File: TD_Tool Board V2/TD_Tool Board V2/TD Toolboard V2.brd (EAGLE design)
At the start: 54.2 x 49 mm, 141 parts, among them J3 430450400CON_430450400_MOL, M1 NMOSFET_WSD3066DN33, M2 CJ3400, M3 CJ3400, M4 CJ3400, P1 TPS54202_BUCKCONV, P2 3.3V, U1 RP2040IC57_RP2040-L, U2 W25Q128JVSIQSOIC_128JVSIQ_WIN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, U3 SN65HVD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

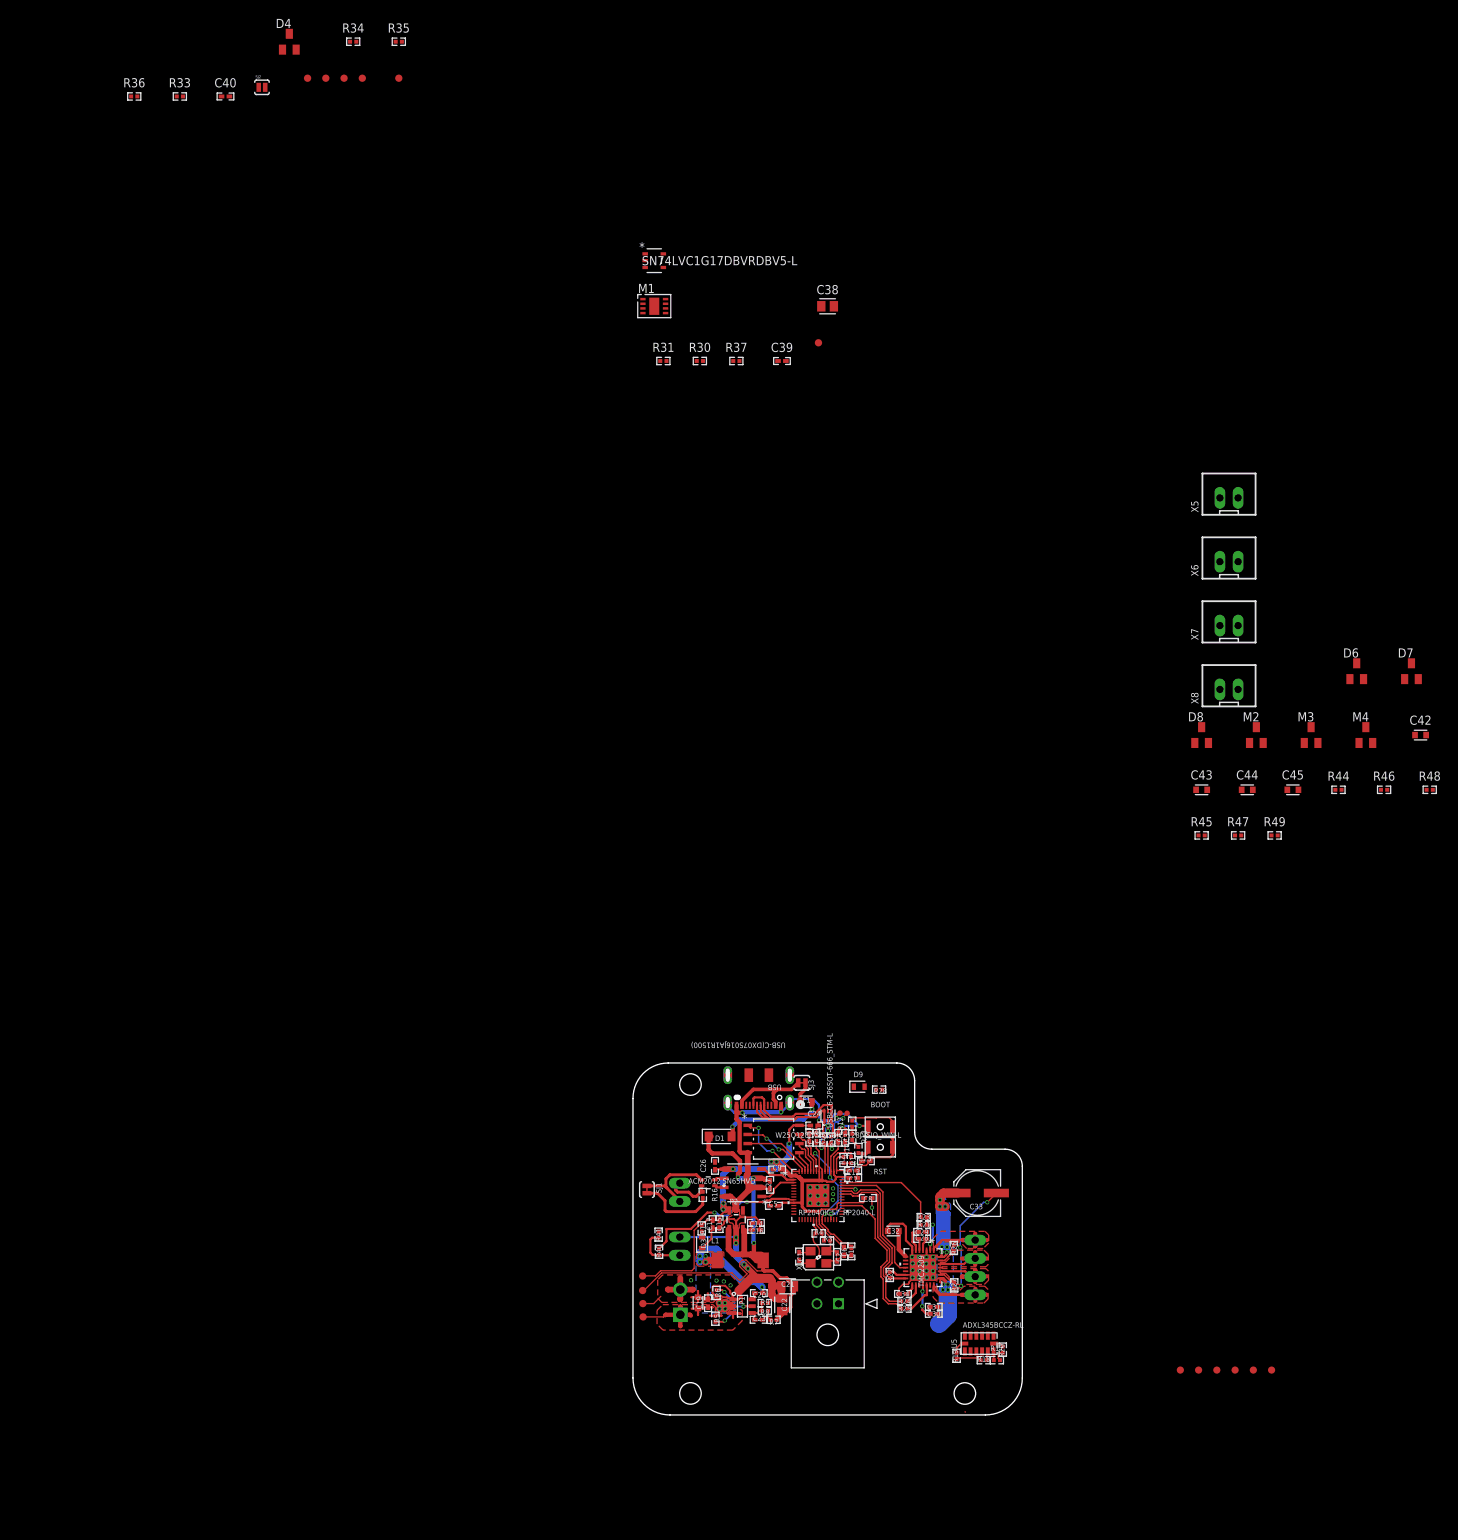
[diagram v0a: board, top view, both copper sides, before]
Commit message: Placed other connectors and re arranged adxl345
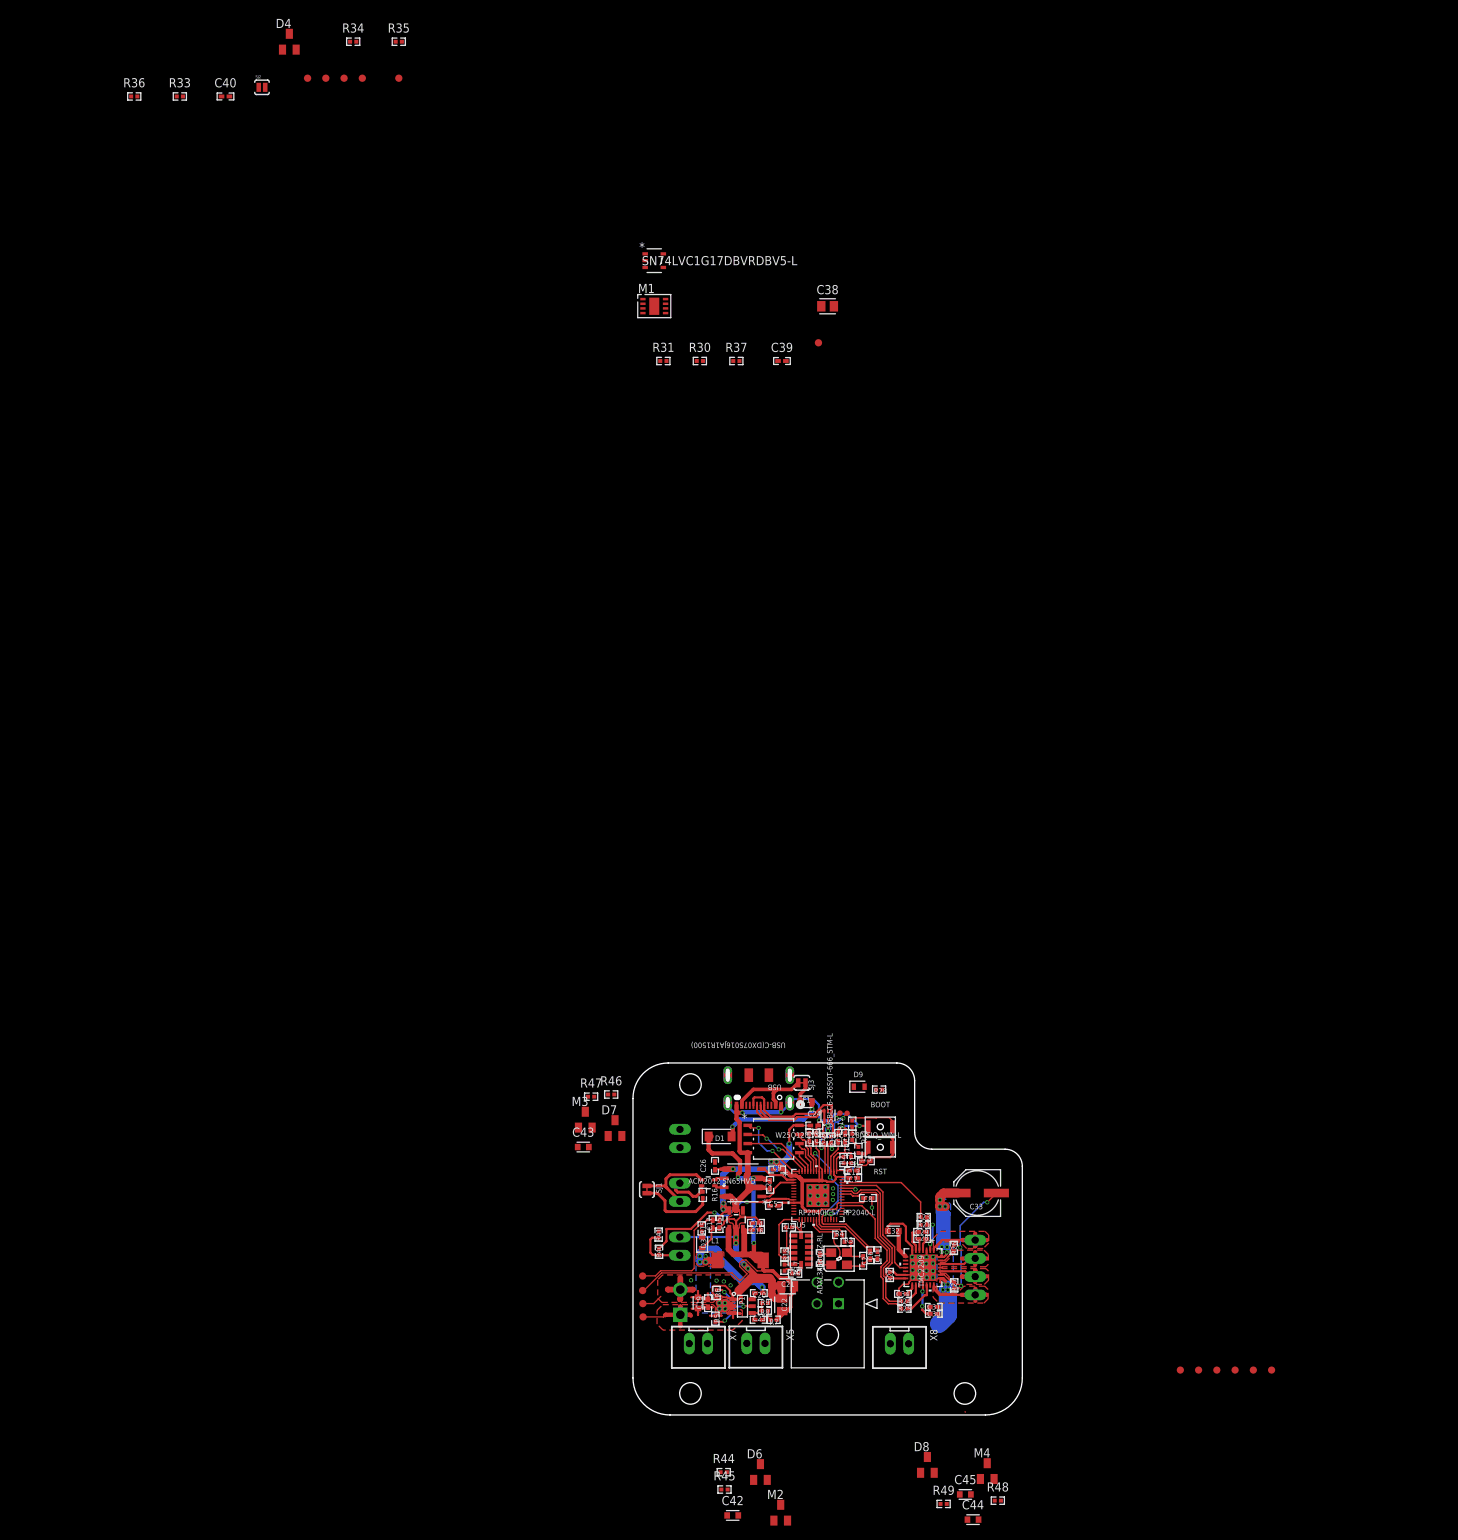
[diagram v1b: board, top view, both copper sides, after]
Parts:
- moved C42 144.8 mm to (104.9, -71.8)
- moved D6 139.0 mm to (108.8, -65.8)
- moved X5 134.9 mm to (108.1, -47.9), turned to 180 degrees
- moved R44 127.9 mm to (103.7, -65.8)
- moved D7 127.8 mm to (88.5, -17.9)
- moved M2 126.9 mm to (111.6, -71.4)
- moved X7 124.3 mm to (100.1, -47.9), turned to 180 degrees
- moved R48 115.8 mm to (141.8, -69.7)
- moved R46 115.7 mm to (88.0, -13.2)
- moved M4 115.2 mm to (140.3, -65.6)
- moved M3 114.4 mm to (84.4, -16.7)
- moved R45 112.7 mm to (103.8, -68.2)
- moved X6 110.8 mm to (97.6, -19.3), flipped to the bottom, turned to 270 degrees
- moved C44 108.5 mm to (138.4, -72.4)
- moved D8 108.5 mm to (132.0, -64.8)
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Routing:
- net SPI1_MISO: track 1.27 -> 9.50 mm
- net +3.3V: track 116.9 -> 120.6 mm
- net +1.1V: track 28.2 -> 31.8 mm
- net OSC_OUT: track 3.29 -> 6.21 mm
- net OSC_IN: track 8.41 -> 10.8 mm
- net SPI1_CS: track 1.95 -> 3.72 mm
- net XR: track 3.26 -> 4.16 mm
- net GND: track 195.9 -> 196.7 mm

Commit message: Finished routing all components
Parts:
- removed FD1, FD2, FD3: FIDUCIAL, CDC Library:FIDUCIAL_1MM
- D9: device LED:LEDC1608X35N_FLAT-G -> led:LED3MM
- moved FD5 178.9 mm to (8.90, 8.55)
- moved FD6 172.4 mm to (41.6, 51.4)
- moved C44 145.2 mm to (17.6, 8.18), turned to 270 degrees
- moved FD4 134.2 mm to (55.2, 9.11)
- moved R48 128.0 mm to (39.9, 7.77), turned to 180 degrees
- moved C45 125.8 mm to (39.5, 10.3)
- moved R49 123.1 mm to (39.9, 8.86), turned to 180 degrees
- moved M4 120.7 mm to (45.6, 9.19)
- moved C42 118.3 mm to (19.8, 10.4), turned to 180 degrees
- moved M2 117.6 mm to (26.0, 9.14)
- moved D8 116.0 mm to (42.6, 9.17), turned to 180 degrees
- moved D6 114.0 mm to (22.9, 9.22), turned to 180 degrees
- moved R45 113.7 mm to (20.0, 8.69), turned to 180 degrees
- moved R20 111.7 mm to (26.4, 31.6)
- moved R44 111.4 mm to (20.0, 7.72), turned to 180 degrees
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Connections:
- net GND: now also D9.K; no longer D9.C
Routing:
- net +3.3V: track 120.6 -> 256.3 mm, vias 6 -> 17
- net +24V: track 45.9 -> 176.4 mm, vias 11 -> 13
- net N$2: track 0.00 -> 38.5 mm
- net HE0: track 0.00 -> 37.2 mm, vias 0 -> 2
- net FAN2: track 0.00 -> 36.6 mm, vias 0 -> 2
- net FAN0: track 0.00 -> 33.2 mm, vias 0 -> 2
- net FAN1: track 0.00 -> 32.8 mm, vias 0 -> 2
- net LED: track 0.00 -> 29.2 mm, vias 0 -> 3
- net TH0: track 1.95 -> 29.3 mm, vias 1 -> 3
- net TH0A: track 0.00 -> 26.6 mm, vias 0 -> 1
- net HE0_PWR: track 0.00 -> 25.7 mm
- net +5V: track 76.5 -> 100.1 mm
- net GND: track 196.7 -> 216.6 mm, vias 49 -> 211
- net QSPI_SS: track 12.0 -> 25.2 mm, vias 2 -> 4
- net FAN1G: track 0.00 -> 8.34 mm
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- added copper zone on layer 1, net HE0_PWR
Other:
- outline, holes or cut-outs redrawn
- board text removed: "Fans"
- board text removed: "Hotend Heater"
- board text removed: "Stepper Driver"
- board text removed: "Toolhead Connectors"
- board text removed: "USB"
- board text removed: "Umblical Connectors"

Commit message: Minor Changes for ground connectivity
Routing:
- net TH0A: track 26.6 -> 23.7 mm
- net +5V: track 100.1 -> 97.3 mm
- net FAN1: track 32.8 -> 34.3 mm
- net +3.3V: track 256.3 -> 255.0 mm
- net GND: track 216.6 -> 216.7 mm, vias 211 -> 213

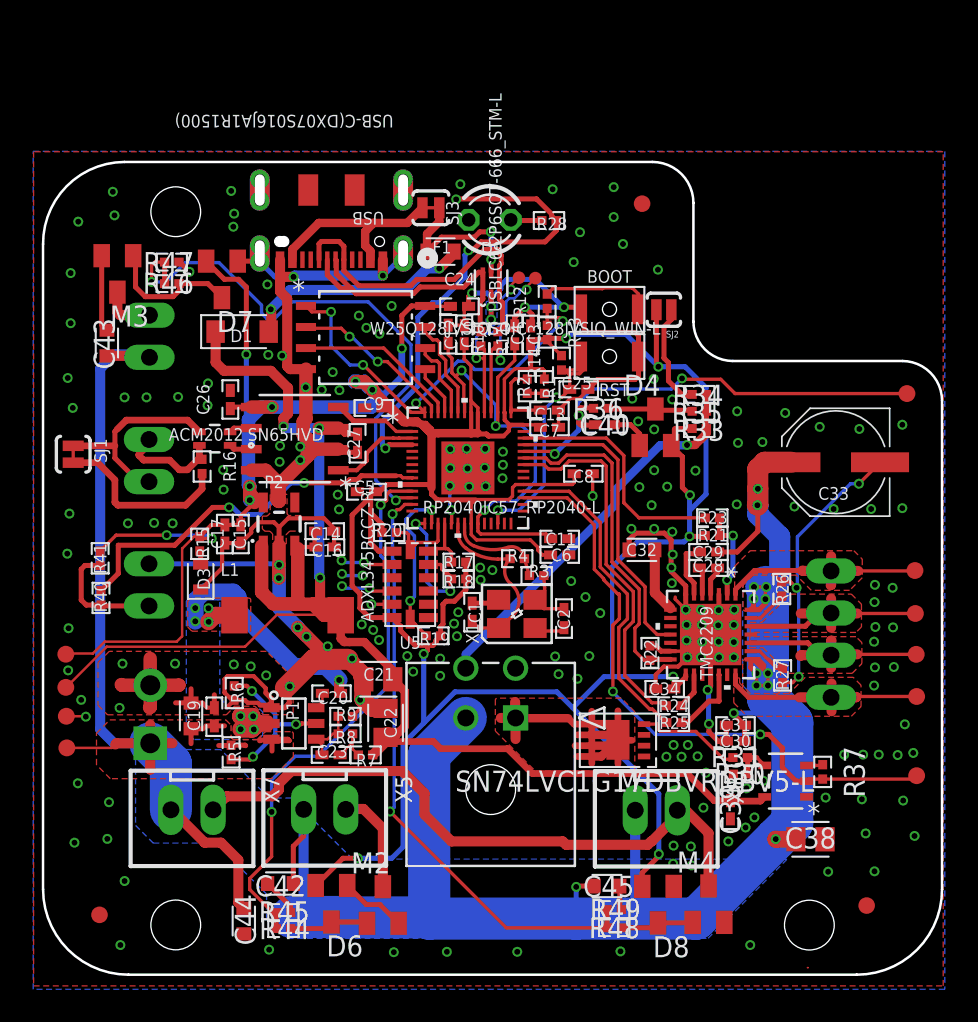
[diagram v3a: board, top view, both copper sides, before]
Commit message: Fixed font sizes, added lables
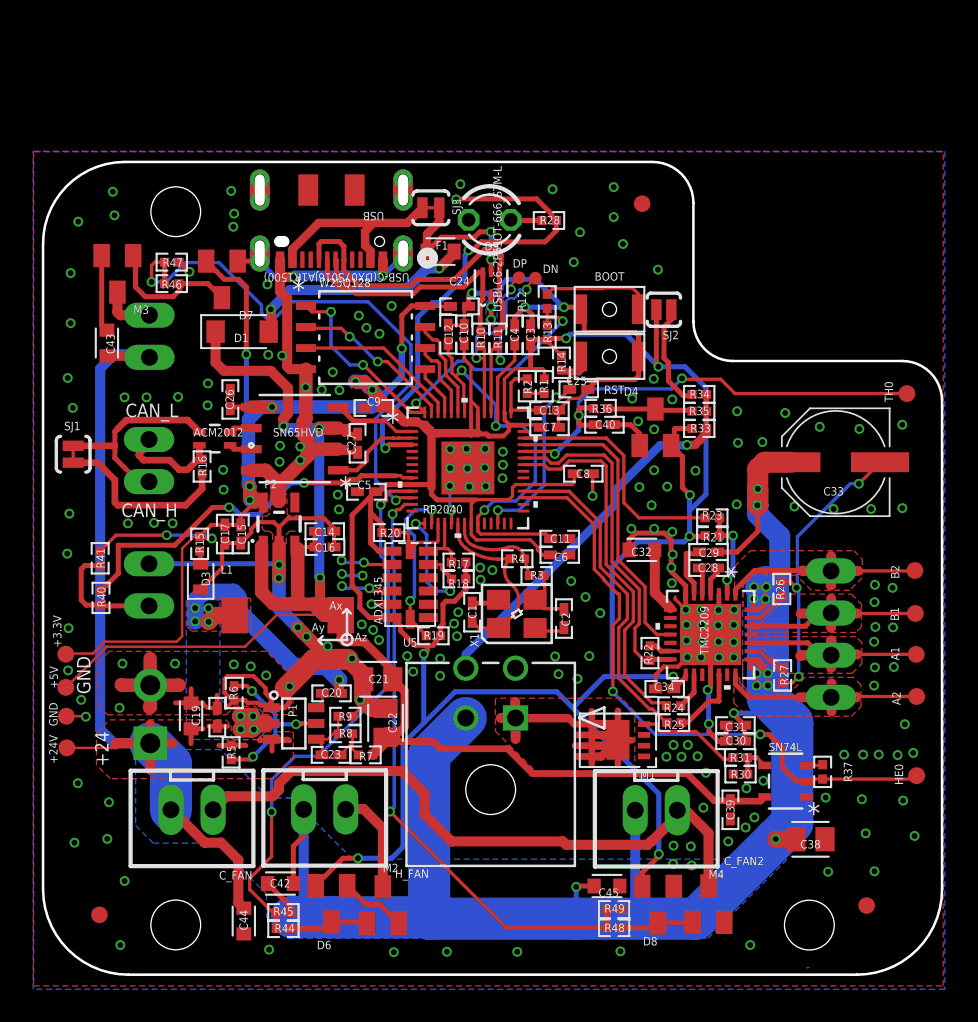
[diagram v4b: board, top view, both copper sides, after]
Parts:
- C_FAN2: value JST-XH-02-PIN-LONG-PAD -> JST-XH
- J3: value 430450400CON_430450400_MOL -> JST-MICROFIT
- U1: value RP2040IC57_RP2040-L -> RP2040
- U2: value W25Q128JVSIQSOIC_128JVSIQ_WIN-L -> W25Q128
- U5: value ADXL345BCCZ-RL -> ADXL345
- U6: value SN74LVC1G17DBVRDBV5-L -> SN74L
- moved C18 0.18 mm to (16.0, 20.5)
- renumbered X2 to CANBUS, X3 to ENDSTOP, X5 to H_FAN, X6 to M_FAN, X7 to C_FAN, X8 to C_FAN2
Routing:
- net GND: track 216.7 -> 215.3 mm
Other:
- board text added: "+24"
- board text added: "+24V"
- board text added: "+3.3V"
- board text added: "+5V"
- board text added: "A1"
- board text added: "A2"
- board text added: "Ax"
- board text added: "Ay"
- board text added: "Az"
- board text added: "B1"
- board text added: "B2"
- board text added: "CAN_H"
- board text added: "CAN_L"
- board text added: "DN"
- board text added: "DP"
- board text added: "GND"
- board text added: "HE0"
- board text added: "TH0"
